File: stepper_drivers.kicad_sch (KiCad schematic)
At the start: 10 parts, among them T1 Stepper Driver (X-Axis), T2 Stepper Driver (Y-Axis), T3 Stepper Driver (Z-Axis)

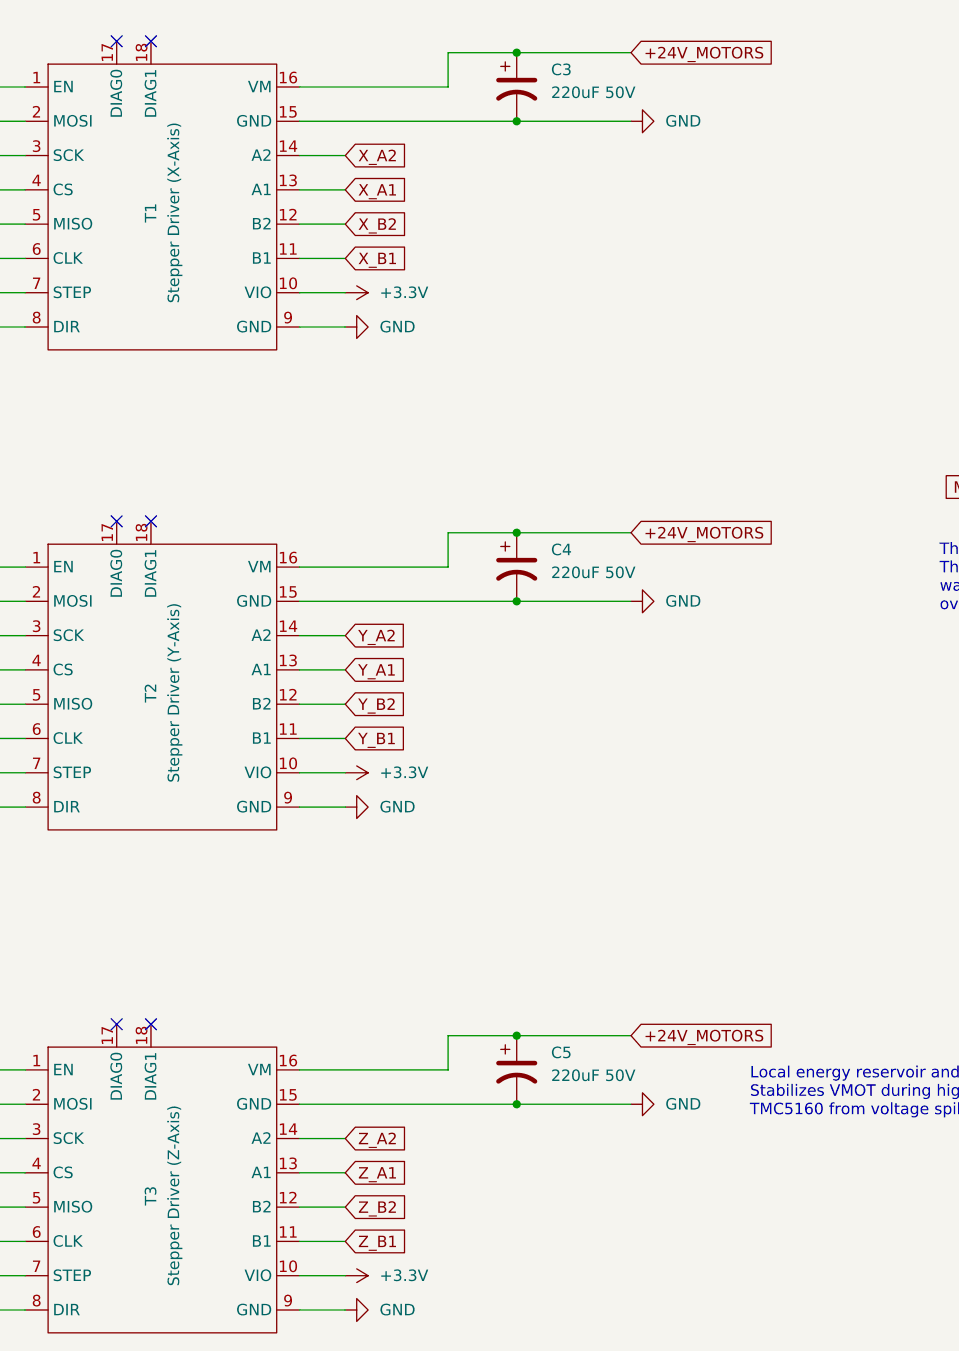
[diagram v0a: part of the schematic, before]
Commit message: rearrange and connect everything
rearrange and connect everything
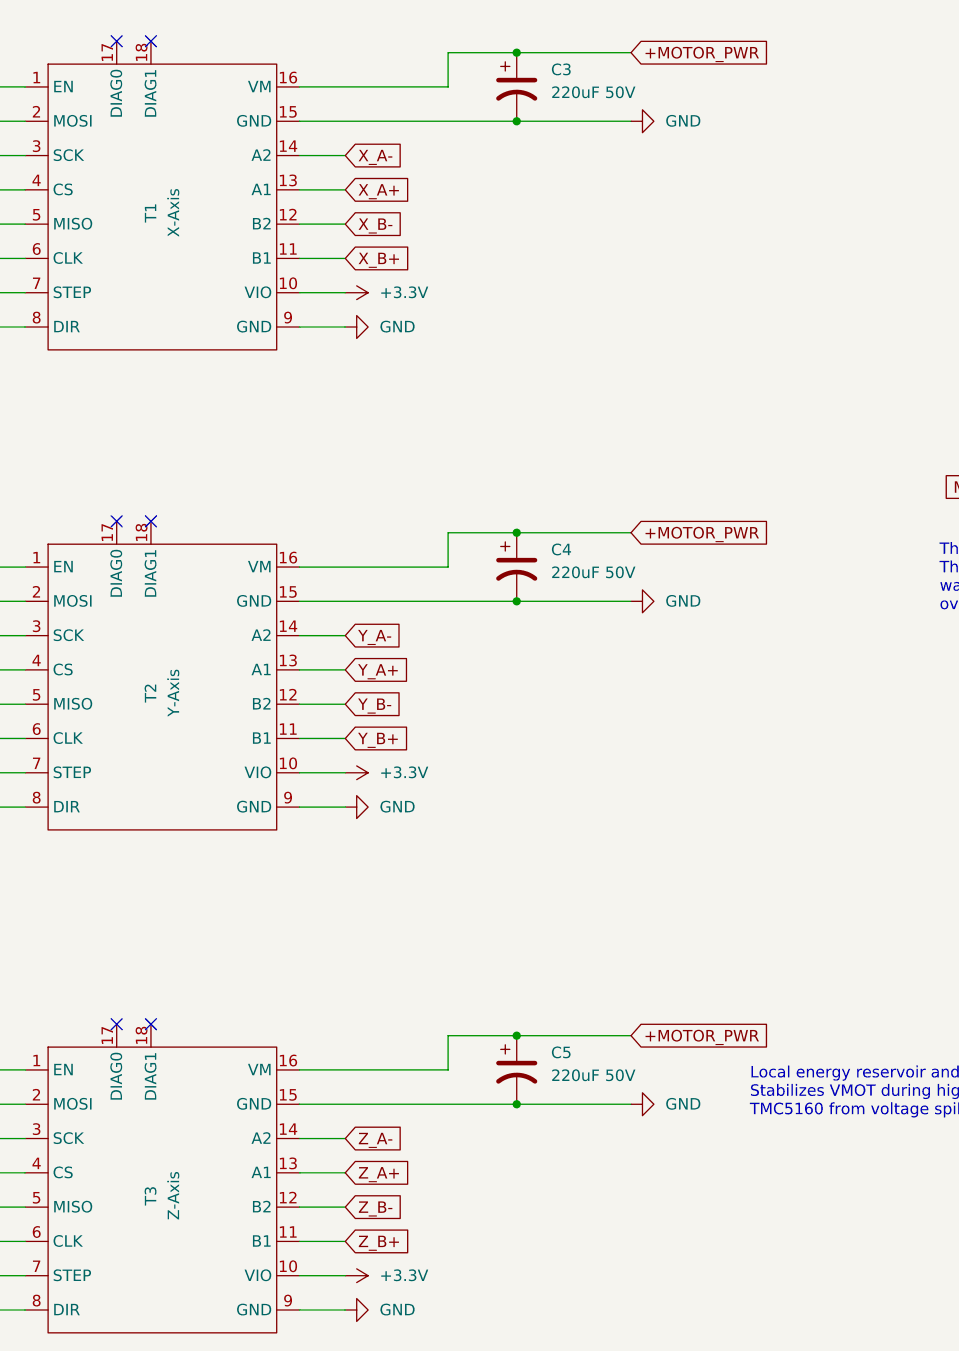
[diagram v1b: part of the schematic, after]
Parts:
- T1: value Stepper Driver (X-Axis) -> X-Axis
- T2: value Stepper Driver (Y-Axis) -> Y-Axis
- T3: value Stepper Driver (Z-Axis) -> Z-Axis
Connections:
- net +24V_MOTORS renamed +MOTOR_PWR
- net X_A1 renamed X_A+
- net X_A2 renamed X_A-
- net X_B1 renamed X_B+
- net X_B2 renamed X_B-
- net Y_A1 renamed Y_A+
- net Y_A2 renamed Y_A-
- net Y_B1 renamed Y_B+
- net Y_B2 renamed Y_B-
- net Z_A1 renamed Z_A+
- net Z_A2 renamed Z_A-
- net Z_B1 renamed Z_B+
- net Z_B2 renamed Z_B-
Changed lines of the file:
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@@
 		)
 	)
-	(global_label "+24V_MOTORS"
+	(global_label "+MOTOR_PWR"
 		(shape input)
 		(at 176.53 26.67 0)
@@
 		)
 	)
-	(global_label "Y_A1"
+	(global_label "Y_A+"
 		(shape input)
 		(at 144.78 95.25 0)
@@
 		)
 	)
-	(global_label "Z_A2"
+	(global_label "Z_A-"
 		(shape input)
 		(at 144.78 147.32 0)
@@
 		)
 	)
-	(global_label "+24V_MOTORS"
+	(global_label "+MOTOR_PWR"
 		(shape input)
 		(at 176.53 135.89 0)
@@
 		)
 	)
-	(global_label "+24V_MOTORS"
+	(global_label "+MOTOR_PWR"
 		(shape input)
 		(at 176.53 80.01 0)
@@
 		)
 	)
-	(global_label "Y_A2"
+	(global_label "Y_A-"
 		(shape input)
 		(at 144.78 91.44 0)
@@
 		)
 	)
-	(global_label "Z_B1"
+	(global_label "Z_B+"
 		(shape input)
 		(at 144.78 158.75 0)
@@
 		)
 	)
-	(global_label "Y_B2"
+	(global_label "Y_B-"
 		(shape input)
 		(at 144.78 99.06 0)
@@
 		)
 	)
-	(global_label "X_A1"
+	(global_label "X_A+"
 		(shape input)
 		(at 144.78 41.91 0)
@@
 		)
 	)
-	(global_label "X_B2"
+	(global_label "X_B-"
 		(shape input)
 		(at 144.78 45.72 0)
@@
 		)
 	)
-	(global_label "Z_A1"
+	(global_label "Z_A+"
 		(shape input)
 		(at 144.78 151.13 0)
@@
 		)
 	)
-	(global_label "Y_B1"
+	(global_label "Y_B+"
 		(shape input)
 		(at 144.78 102.87 0)
@@
 		)
 	)
-	(global_label "X_A2"
+	(global_label "X_A-"
 		(shape input)
 		(at 144.78 38.1 0)
@@
 		)
 	)
-	(global_label "Z_B2"
+	(global_label "Z_B-"
 		(shape input)
 		(at 144.78 154.94 0)
@@
 		)
 	)
-	(global_label "X_B1"
+	(global_label "X_B+"
 		(shape input)
 		(at 144.78 49.53 0)
@@
 			)
 		)
-		(property "Value" "Stepper Driver (X-Axis)"
+		(property "Value" "X-Axis"
 			(at 125.73 44.45 90)
 			(effects
@@
 			)
 		)
-		(property "Value" "Stepper Driver (Y-Axis)"
+		(property "Value" "Y-Axis"
 			(at 125.73 97.79 90)
 			(effects
@@
 			)
 		)
-		(property "Value" "Stepper Driver (Z-Axis)"
+		(property "Value" "Z-Axis"
 			(at 125.73 153.67 90)
 			(effects
